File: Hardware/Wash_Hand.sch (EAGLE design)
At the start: 86 parts, among them IC1 LM358D, IC2 LP298XS, IC3 405016TSSOP, J1 I2C, J2 ICSP, J3 SPI, J4 9V_CONN, J5 EXT_VCC, J6 6_PIN_SERIAL_CABLEPTH, Q1 16.0 Mhz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

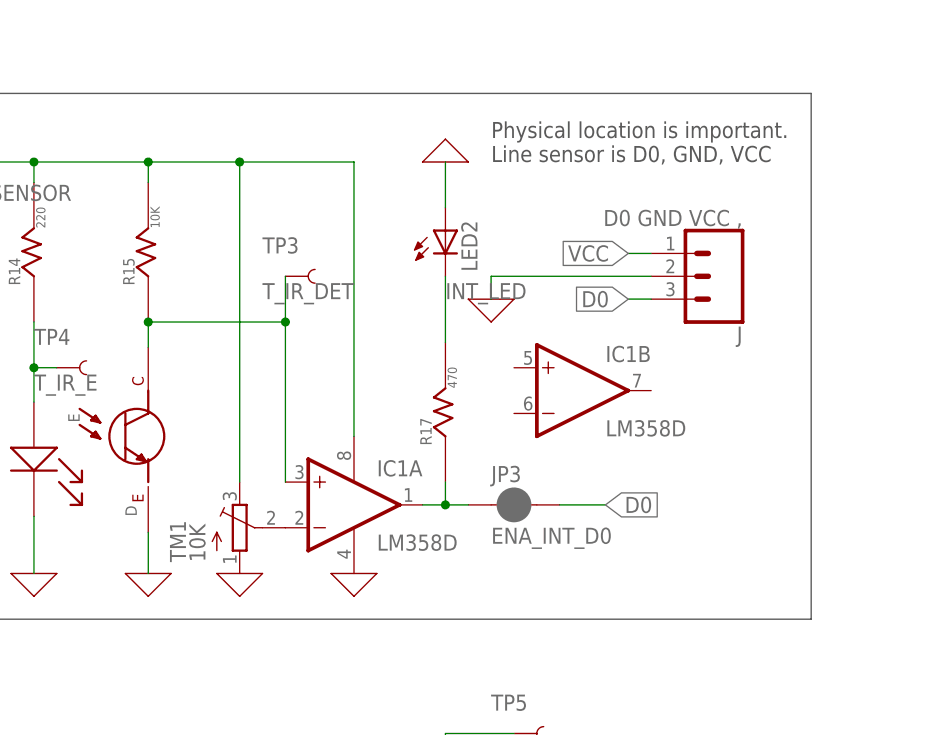
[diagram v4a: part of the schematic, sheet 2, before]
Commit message: Board/Schematic: Add 3connector to LM358D and add names
.. to the wires to make it more obvious on the schematic.

Signed-off-by: Konrad Rzeszutek Wilk <konrad@kernel.org>
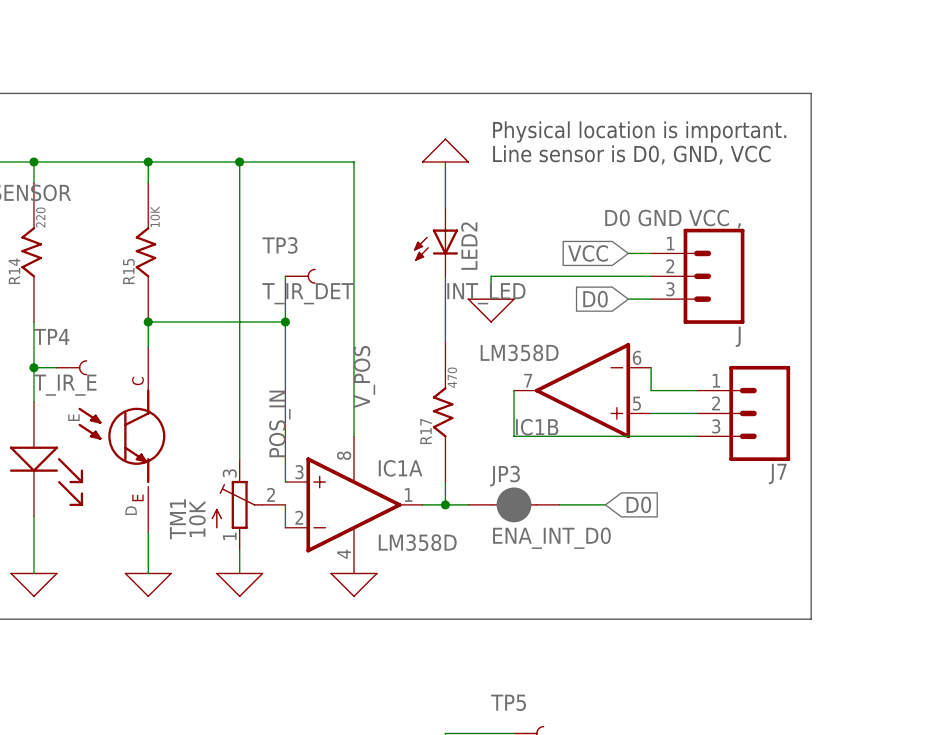
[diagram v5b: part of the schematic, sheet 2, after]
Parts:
- added J7: (no value), SparkFun-Connectors:CONN_03
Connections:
- net N$14 renamed POS_IN
- net N$15 renamed V_POS
- net N$16 renamed NEG_IN
- new net N$1: IC1B.OUT, J7.3
- new net N$14: IC1B.-IN, J7.1
- new net N$9: IC1B.+IN, J7.2
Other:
- moved on the sheet: IC1B, TM1
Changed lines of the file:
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@@
 <part name="C16" library="SparkFun-Capacitors" library_urn="urn:adsk.eagle:library:510" deviceset="10UF" device="-1206-6.3V-20%" package3d_urn="urn:adsk.eagle:package:37426/1" value="0.1uF"/>
 <part name="X_36" library="ngspice-simulation" library_urn="urn:adsk.eagle:library:527439" deviceset="GND" device=""/>
+<part name="J7" library="SparkFun-Connectors" library_urn="urn:adsk.eagle:library:513" deviceset="CONN_03" device="" package3d_urn="urn:adsk.eagle:package:38063/1"/>
 </parts>
 <sheets>
@@
 <attribute name="VALUE" x="193.04" y="127" size="1.778" layer="96"/>
 </instance>
-<instance part="TM1" gate="G$1" x="177.8" y="129.54" smashed="yes">
-<attribute name="NAME" x="171.831" y="125.73" size="1.778" layer="95" rot="R90"/>
-<attribute name="VALUE" x="173.99" y="125.73" size="1.778" layer="96" rot="R90"/>
+<instance part="TM1" gate="G$1" x="177.8" y="132.08" smashed="yes">
+<attribute name="NAME" x="171.831" y="128.27" size="1.778" layer="95" rot="R90"/>
+<attribute name="VALUE" x="173.99" y="128.27" size="1.778" layer="96" rot="R90"/>
 </instance>
 <instance part="E" gate="G$1" x="154.94" y="137.16" smashed="yes" rot="R270">
@@
 <instance part="IC1" gate="P" x="190.5" y="132.08" smashed="yes"/>
 <instance part="X_1" gate="G$1" x="190.5" y="124.46" smashed="yes"/>
-<instance part="IC1" gate="B" x="215.9" y="144.78" smashed="yes">
-<attribute name="NAME" x="218.44" y="147.955" size="1.778" layer="95"/>
-<attribute name="VALUE" x="218.44" y="139.7" size="1.778" layer="96"/>
+<instance part="IC1" gate="B" x="215.9" y="144.78" smashed="yes" rot="R180">
+<attribute name="NAME" x="213.36" y="141.605" size="1.778" layer="95" rot="R180"/>
+<attribute name="VALUE" x="213.36" y="149.86" size="1.778" layer="96" rot="R180"/>
 </instance>
 <instance part="R17" gate="G$1" x="200.66" y="139.7" smashed="yes" rot="R90">
@@
 <attribute name="NAME" x="57.404" y="184.404" size="1.27" layer="95"/>
 <attribute name="VALUE" x="63.754" y="181.61" size="1.016" layer="96"/>
+</instance>
+<instance part="J7" gate="J$1" x="236.22" y="142.24" smashed="yes" rot="R180">
+<attribute name="VALUE" x="238.76" y="149.606" size="1.778" layer="96" font="vector" rot="R180"/>
+<attribute name="NAME" x="238.76" y="136.652" size="1.778" layer="95" font="vector" rot="R180"/>
 </instance>
 </instances>
@@
 <pinref part="TM1" gate="G$1" pin="A"/>
 <pinref part="X_16" gate="G$1" pin="0"/>
+<wire x1="177.8" y1="127" x2="177.8" y2="124.46" width="0.1524" layer="91"/>
 </segment>
 <segment>
@@
 </segment>
 </net>
-<net name="N$15" class="0">
+<net name="V_POS" class="0">
 <segment>
 <pinref part="JP4" gate="G$1" pin="2"/>
@@
 <wire x1="167.64" y1="170.18" x2="167.64" y2="167.894" width="0.1524" layer="91"/>
 <pinref part="TM1" gate="G$1" pin="E"/>
-<wire x1="177.8" y1="134.62" x2="177.8" y2="170.18" width="0.1524" layer="91"/>
+<wire x1="177.8" y1="137.16" x2="177.8" y2="170.18" width="0.1524" layer="91"/>
 <wire x1="177.8" y1="170.18" x2="167.64" y2="170.18" width="0.1524" layer="91"/>
 <junction x="167.64" y="170.18"/>
@@
 <wire x1="190.5" y1="170.18" x2="177.8" y2="170.18" width="0.1524" layer="91"/>
 <junction x="177.8" y="170.18"/>
-</segment>
-</net>
-<net name="N$16" class="0">
+<label x="190.5" y="149.86" size="1.778" layer="95" rot="R270"/>
+</segment>
+</net>
+<net name="NEG_IN" class="0">
 <segment>
 <pinref part="TM1" gate="G$1" pin="S"/>
 <pinref part="IC1" gate="A" pin="-IN"/>
-</segment>
-</net>
-<net name="N$14" class="0">
+<wire x1="182.88" y1="132.08" x2="182.88" y2="129.54" width="0.1524" layer="91"/>
+</segment>
+</net>
+<net name="POS_IN" class="0">
 <segment>
 <wire x1="182.88" y1="152.4" x2="182.88" y2="134.62" width="0.1524" layer="91"/>
@@
 <wire x1="182.88" y1="152.4" x2="182.88" y2="157.48" width="0.1524" layer="91"/>
 <junction x="182.88" y="152.4"/>
+<label x="182.88" y="137.16" size="1.778" layer="95" rot="R90"/>
 </segment>
 </net>
@@
 </segment>
 </net>
+<net name="N$1" class="0">
+<segment>
+<pinref part="IC1" gate="B" pin="OUT"/>
+<wire x1="208.28" y1="144.78" x2="208.28" y2="139.7" width="0.1524" layer="91"/>
+<pinref part="J7" gate="J$1" pin="3"/>
+<wire x1="208.28" y1="139.7" x2="228.6" y2="139.7" width="0.1524" layer="91"/>
+</segment>
+</net>
+<net name="N$9" class="0">
+<segment>
+<pinref part="IC1" gate="B" pin="+IN"/>
+<pinref part="J7" gate="J$1" pin="2"/>
+<wire x1="223.52" y1="142.24" x2="228.6" y2="142.24" width="0.1524" layer="91"/>
+</segment>
+</net>
+<net name="N$14" class="0">
+<segment>
+<pinref part="IC1" gate="B" pin="-IN"/>
+<pinref part="J7" gate="J$1" pin="1"/>
+<wire x1="223.52" y1="147.32" x2="223.52" y2="144.78" width="0.1524" layer="91"/>
+<wire x1="223.52" y1="144.78" x2="228.6" y2="144.78" width="0.1524" layer="91"/>
+</segment>
+</net>

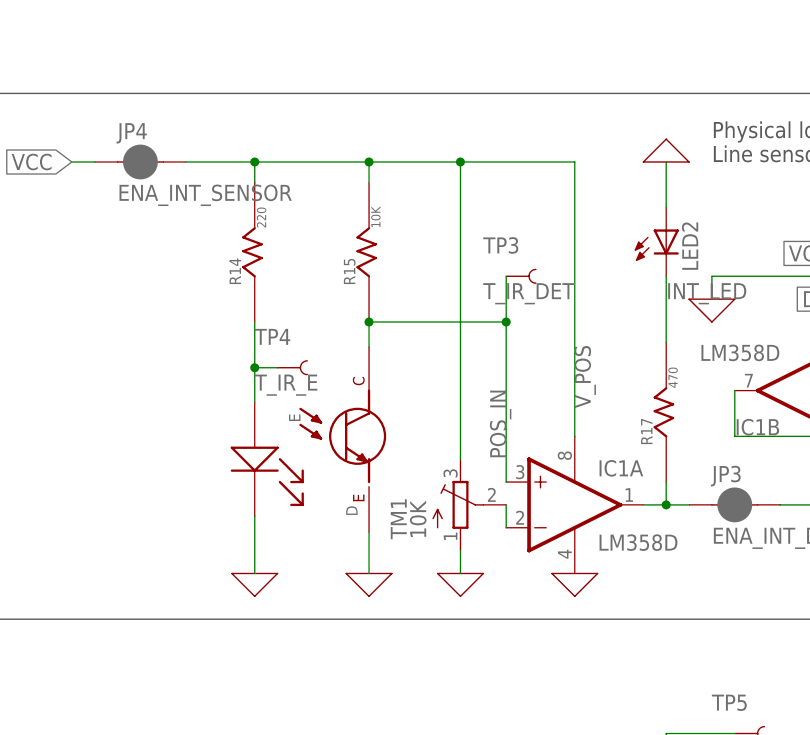
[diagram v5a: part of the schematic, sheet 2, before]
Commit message: Board/Schematic: Line Sensor: Swap 10K with PIR sensor
I had the 10K with PIR sensor inverted. That is
the voltage would go down when we are in dark room (so
nothing to detect), and go above the Vref (aka the
10K pot on NEG_IN) and light up the LED.

We need it the other way around - that is in dark
rooms (so PIR is 20K ohm ,or 7.8K ohm) we want the
voltage to be below the Vref (NEG_IN), and only go
high when the 940nm light emitter is reflected and
PIR is around 300ohm.

PIR ohm| 10K | voltage|conditions
---+-----+------------+----------
300    | 10K | 4.8V   | light reflected
7.8K   | 10K | 3.6V   | daylight
20K    | 10K | 1.6V   | dark night

Signed-off-by: Konrad Rzeszutek Wilk <konrad@kernel.org>
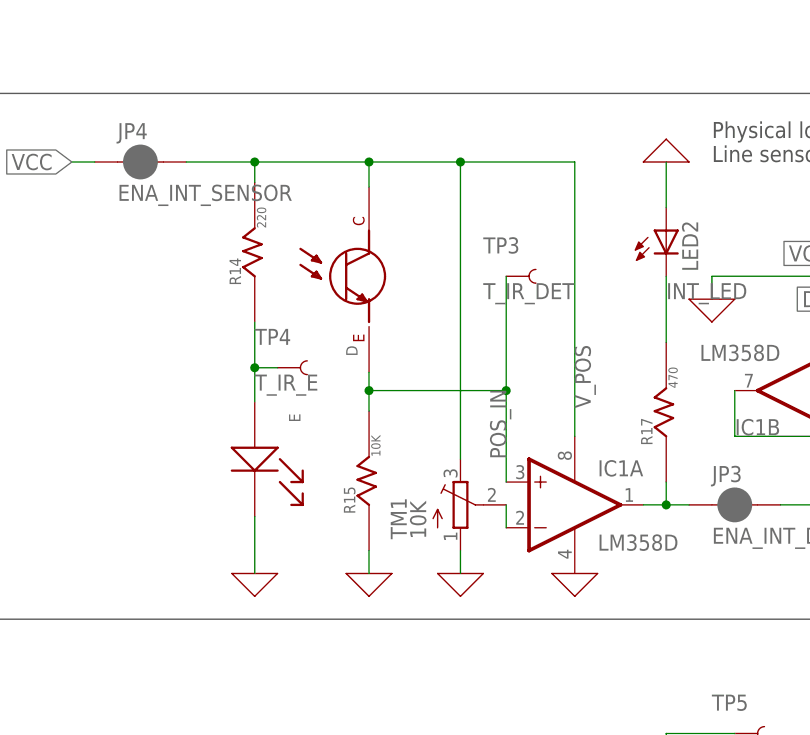
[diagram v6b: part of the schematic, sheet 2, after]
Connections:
- net 0: now also R15.R_1; no longer D.E$1
- net POS_IN: now also D.E$1, R15.R_2; no longer D.C$1, R15.R_1
- net V_POS: now also D.C$1; no longer R15.R_2
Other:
- moved on the sheet: D, R15
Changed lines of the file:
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@@
 <attribute name="VALUE" x="139.7" y="167.64" size="1.778" layer="96" font="vector" align="top-left"/>
 </instance>
-<instance part="R15" gate="G$1" x="167.64" y="157.48" smashed="yes" rot="R90">
-<attribute name="NAME" x="166.116" y="156.464" size="1.27" layer="95" rot="R90"/>
-<attribute name="VALUE" x="168.91" y="162.814" size="1.016" layer="96" rot="R90"/>
+<instance part="R15" gate="G$1" x="167.64" y="132.08" smashed="yes" rot="R90">
+<attribute name="NAME" x="166.116" y="131.064" size="1.27" layer="95" rot="R90"/>
+<attribute name="VALUE" x="168.91" y="137.414" size="1.016" layer="96" rot="R90"/>
 </instance>
 <instance part="X_14" gate="G$1" x="154.94" y="124.46" smashed="yes"/>
@@
 <attribute name="NAME" x="158.75" y="142.24" size="1.27" layer="95" rot="R270"/>
 </instance>
-<instance part="D" gate="G$1" x="167.64" y="139.7" smashed="yes" rot="R90">
-<attribute name="NAME" x="166.37" y="130.81" size="1.27" layer="95" rot="R90"/>
+<instance part="D" gate="G$1" x="167.64" y="157.48" smashed="yes" rot="R90">
+<attribute name="NAME" x="166.37" y="148.59" size="1.27" layer="95" rot="R90"/>
 </instance>
 <instance part="X_16" gate="G$1" x="177.8" y="124.46" smashed="yes"/>
@@
 <pinref part="E" gate="G$1" pin="K$1"/>
 <wire x1="154.94" y1="124.46" x2="154.94" y2="130.81" width="0.1524" layer="91"/>
-</segment>
-<segment>
-<pinref part="D" gate="G$1" pin="E$1"/>
-<pinref part="X_15" gate="G$1" pin="0"/>
-<wire x1="167.64" y1="129.032" x2="167.64" y2="124.46" width="0.1524" layer="91"/>
 </segment>
 <segment>
@@
 <wire x1="200.66" y1="170.18" x2="200.66" y2="165.1" width="0.1524" layer="91"/>
 </segment>
+<segment>
+<pinref part="R15" gate="G$1" pin="R_1"/>
+<pinref part="X_15" gate="G$1" pin="0"/>
+<wire x1="167.64" y1="127" x2="167.64" y2="124.46" width="0.1524" layer="91"/>
+</segment>
 </net>
 <net name="D0" class="0">
@@
 <segment>
 <pinref part="JP4" gate="G$1" pin="2"/>
-<pinref part="R15" gate="G$1" pin="R_2"/>
 <wire x1="147.32" y1="170.18" x2="154.94" y2="170.18" width="0.1524" layer="91"/>
 <wire x1="154.94" y1="170.18" x2="167.64" y2="170.18" width="0.1524" layer="91"/>
-<wire x1="167.64" y1="170.18" x2="167.64" y2="167.894" width="0.1524" layer="91"/>
 <pinref part="TM1" gate="G$1" pin="E"/>
+<wire x1="167.64" y1="170.18" x2="177.8" y2="170.18" width="0.1524" layer="91"/>
 <wire x1="177.8" y1="137.16" x2="177.8" y2="170.18" width="0.1524" layer="91"/>
-<wire x1="177.8" y1="170.18" x2="167.64" y2="170.18" width="0.1524" layer="91"/>
-<junction x="167.64" y="170.18"/>
 <pinref part="R14" gate="G$1" pin="R_2"/>
 <wire x1="154.94" y1="167.894" x2="154.94" y2="170.18" width="0.1524" layer="91"/>
@@
 <junction x="177.8" y="170.18"/>
 <label x="190.5" y="149.86" size="1.778" layer="95" rot="R270"/>
+<pinref part="D" gate="G$1" pin="C$1"/>
+<wire x1="167.64" y1="167.386" x2="167.64" y2="170.18" width="0.1524" layer="91"/>
+<junction x="167.64" y="170.18"/>
 </segment>
 </net>
@@
 <net name="POS_IN" class="0">
 <segment>
-<wire x1="182.88" y1="152.4" x2="182.88" y2="134.62" width="0.1524" layer="91"/>
+<wire x1="182.88" y1="157.48" x2="182.88" y2="144.78" width="0.1524" layer="91"/>
 <pinref part="IC1" gate="A" pin="+IN"/>
-<pinref part="D" gate="G$1" pin="C$1"/>
-<pinref part="R15" gate="G$1" pin="R_1"/>
-<wire x1="167.64" y1="149.606" x2="167.64" y2="152.4" width="0.1524" layer="91"/>
-<wire x1="182.88" y1="152.4" x2="167.64" y2="152.4" width="0.1524" layer="91"/>
-<junction x="167.64" y="152.4"/>
 <pinref part="TP3" gate="G$1" pin="1"/>
-<wire x1="182.88" y1="152.4" x2="182.88" y2="157.48" width="0.1524" layer="91"/>
-<junction x="182.88" y="152.4"/>
 <label x="182.88" y="137.16" size="1.778" layer="95" rot="R90"/>
-</segment>
-</net>
+<pinref part="D" gate="G$1" pin="E$1"/>
+<pinref part="R15" gate="G$1" pin="R_2"/>
+<wire x1="182.88" y1="144.78" x2="182.88" y2="134.62" width="0.1524" layer="91"/>
+<wire x1="167.64" y1="142.494" x2="167.64" y2="144.78" width="0.1524" layer="91"/>
+<wire x1="167.64" y1="144.78" x2="167.64" y2="146.812" width="0.1524" layer="91"/>
+<wire x1="167.64" y1="144.78" x2="182.88" y2="144.78" width="0.1524" layer="91"/>
+<junction x="167.64" y="144.78"/>
+<junction x="182.88" y="144.78"/>
+</segment>
+</net>

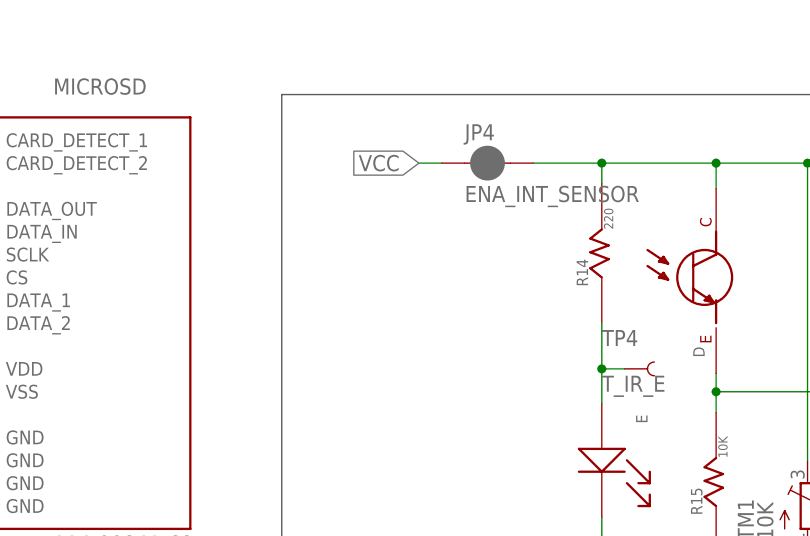
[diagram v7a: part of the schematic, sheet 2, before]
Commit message: Board/Schematic: Add PNP to turn on/off the line sensor
.. which we don't have to have on all the time.

Signed-off-by: Konrad Rzeszutek Wilk <konrad@kernel.org>
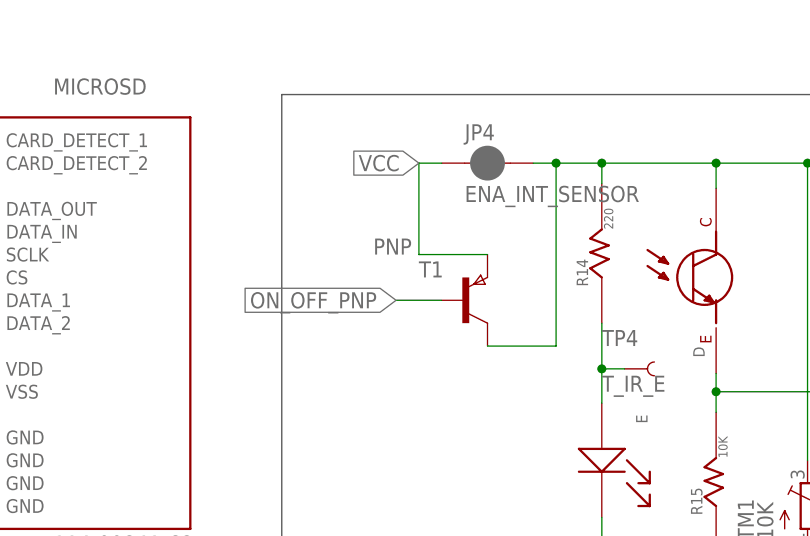
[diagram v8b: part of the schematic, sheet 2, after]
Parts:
- added T1: PNP, zetex:PNPSOT23
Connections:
- new net ON_OFF_PNP: T1.B, U2.ADC7
- net VCC: now also T1.E
- net V_POS: now also T1.C
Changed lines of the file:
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@@
 <part name="X_36" library="ngspice-simulation" library_urn="urn:adsk.eagle:library:527439" deviceset="GND" device=""/>
 <part name="J7" library="SparkFun-Connectors" library_urn="urn:adsk.eagle:library:513" deviceset="CONN_03" device="" package3d_urn="urn:adsk.eagle:package:38063/1"/>
+<part name="T1" library="zetex" library_urn="urn:adsk.eagle:library:418" deviceset="PNPSOT23" device="" package3d_urn="urn:adsk.eagle:package:30981/1" value="PNP"/>
 </parts>
 <sheets>
@@
 <pinref part="JP6" gate="G$1" pin="1"/>
 <wire x1="45.72" y1="96.52" x2="45.72" y2="99.06" width="0.1524" layer="91"/>
+</segment>
+</net>
+<net name="ON_OFF_PNP" class="0">
+<segment>
+<pinref part="U2" gate="U$1" pin="ADC7"/>
+<wire x1="185.42" y1="139.7" x2="187.96" y2="139.7" width="0.1524" layer="91"/>
+<label x="187.96" y="139.7" size="1.778" layer="95" xref="yes"/>
 </segment>
 </net>
@@
 <attribute name="NAME" x="238.76" y="136.652" size="1.778" layer="95" font="vector" rot="R180"/>
 </instance>
+<instance part="T1" gate="A" x="139.7" y="154.94" smashed="yes">
+<attribute name="NAME" x="134.62" y="157.48" size="1.778" layer="95"/>
+<attribute name="VALUE" x="129.54" y="160.02" size="1.778" layer="96"/>
+</instance>
 </instances>
 <busses>
@@
 <wire x1="137.16" y1="170.18" x2="134.62" y2="170.18" width="0.1524" layer="91"/>
 <label x="134.62" y="170.18" size="1.778" layer="95" rot="R180" xref="yes"/>
+<pinref part="T1" gate="A" pin="E"/>
+<wire x1="142.24" y1="160.02" x2="134.62" y2="160.02" width="0.1524" layer="91"/>
+<wire x1="134.62" y1="160.02" x2="134.62" y2="170.18" width="0.1524" layer="91"/>
 </segment>
 <segment>
@@
 <segment>
 <pinref part="JP4" gate="G$1" pin="2"/>
-<wire x1="147.32" y1="170.18" x2="154.94" y2="170.18" width="0.1524" layer="91"/>
+<wire x1="147.32" y1="170.18" x2="149.86" y2="170.18" width="0.1524" layer="91"/>
+<wire x1="149.86" y1="170.18" x2="154.94" y2="170.18" width="0.1524" layer="91"/>
 <wire x1="154.94" y1="170.18" x2="167.64" y2="170.18" width="0.1524" layer="91"/>
 <pinref part="TM1" gate="G$1" pin="E"/>
@@
 <wire x1="167.64" y1="167.386" x2="167.64" y2="170.18" width="0.1524" layer="91"/>
 <junction x="167.64" y="170.18"/>
+<pinref part="T1" gate="A" pin="C"/>
+<wire x1="142.24" y1="149.86" x2="149.86" y2="149.86" width="0.1524" layer="91"/>
+<wire x1="149.86" y1="149.86" x2="149.86" y2="170.18" width="0.1524" layer="91"/>
+<junction x="149.86" y="170.18"/>
 </segment>
 </net>
@@
 </segment>
 </net>
+<net name="ON_OFF_PNP" class="0">
+<segment>
+<pinref part="T1" gate="A" pin="B"/>
+<wire x1="137.16" y1="154.94" x2="132.08" y2="154.94" width="0.1524" layer="91"/>
+<label x="132.08" y="154.94" size="1.778" layer="95" rot="R180" xref="yes"/>
+</segment>
+</net>
